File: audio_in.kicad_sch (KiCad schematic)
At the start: 17 parts, among them SW1 SW_SPDT

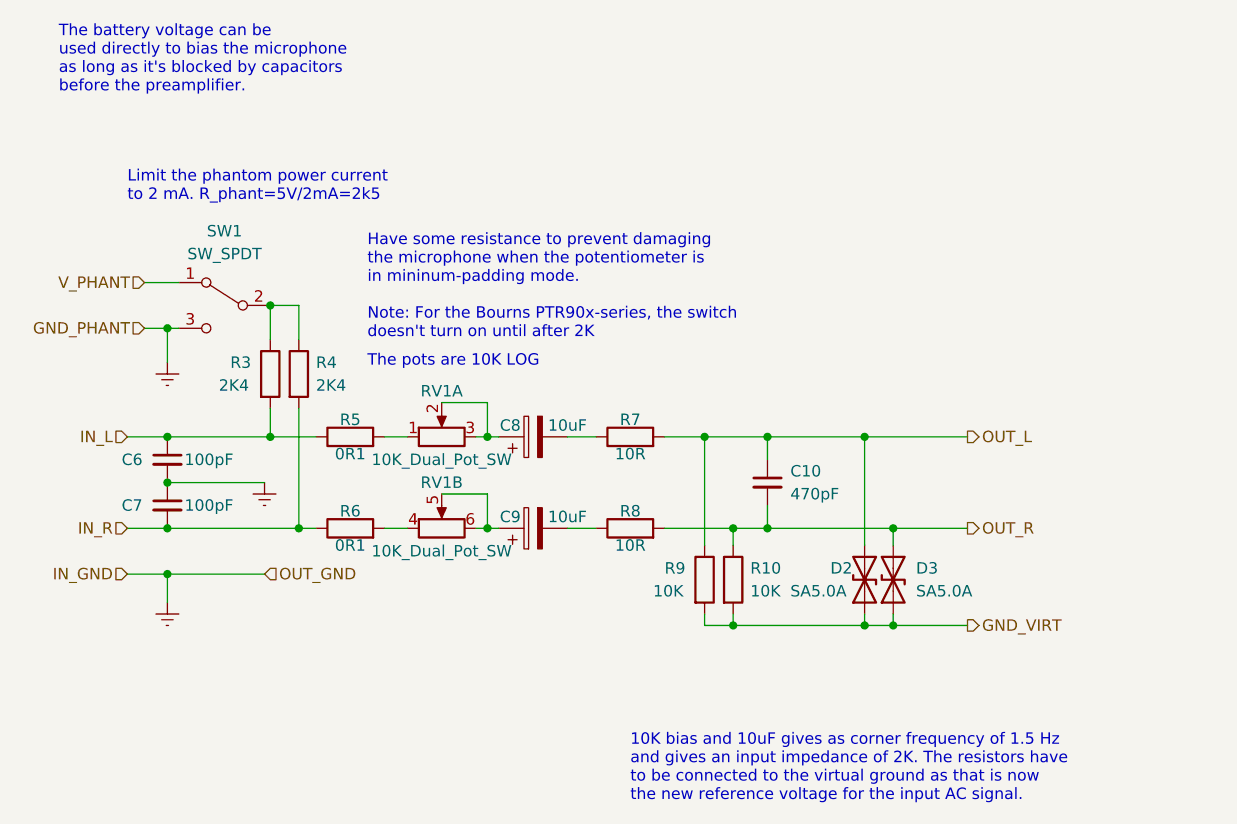
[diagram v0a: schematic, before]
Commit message: Almost finished 2-layer routing, not sure about power/ground layers though
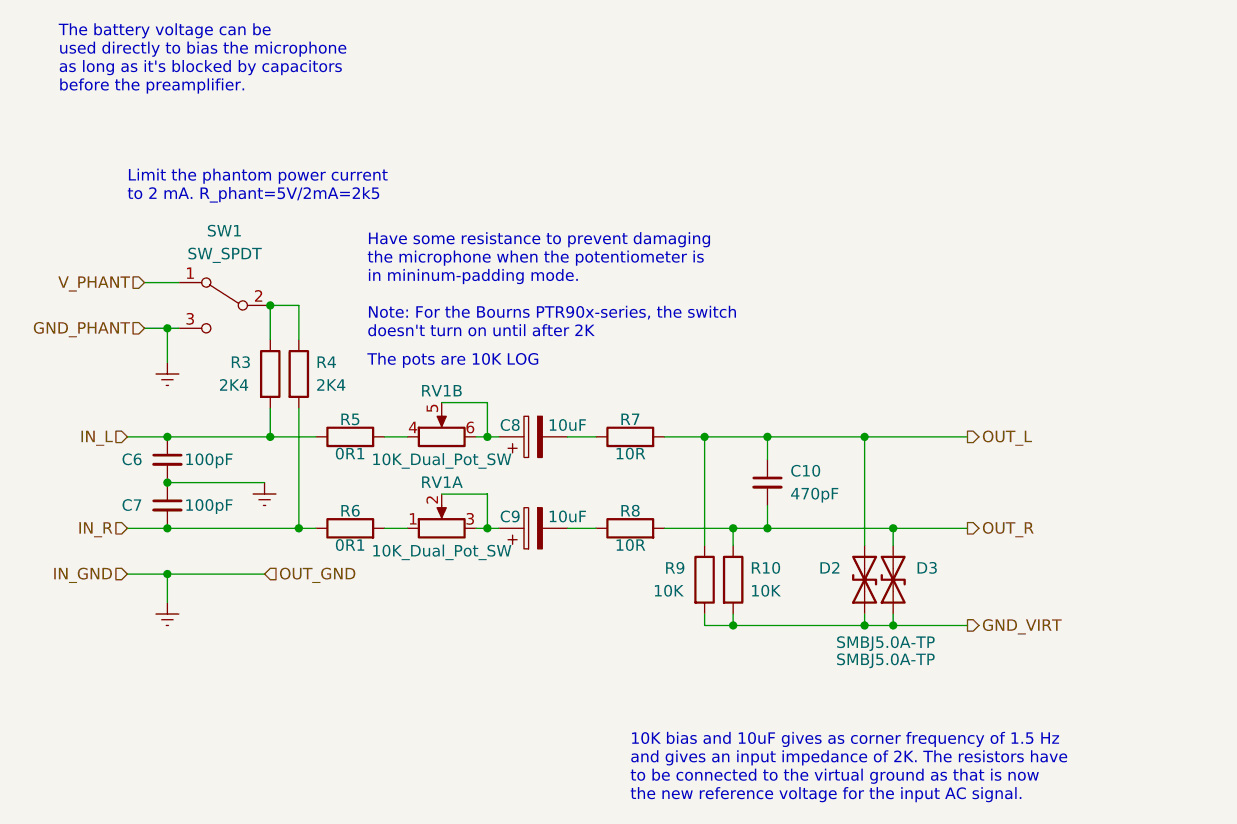
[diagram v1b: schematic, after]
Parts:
- removed D2, D3: SA5.0A, Diode_THT:D_5KP_P7.62mm_Vertical_KathodeUp, symbol preamp_lib:SA5.0A
- added D2, D3: SMBJ5.0A-TP, Diode_SMD:D_SMB_Handsoldering, symbol preamp_lib:SA9.0CA
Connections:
- net GND_VIRT: now also D2.1 (A1), D3.1 (A1)
- net OUT_L: now also D2.2 (A2)
- net OUT_R: now also D3.2 (A2)
- net at RV1.5, RV1.6: now also C8.1; no longer C9.1
- net at R6.2: now also RV1.1 (8); no longer RV1.4
- net at R5.2: now also RV1.4; no longer RV1.1 (8)
- net at RV1.2, RV1.3 (7): now also C9.1; no longer C8.1
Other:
- moved on the sheet: RV1A, RV1B
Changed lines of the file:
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@@
+    (pin "2")
+  )
+  (symbol (lib_id "preamp_lib:SA9.0CA") (at 132.08 81.28 90) (unit 1)
+    (in_bom yes) (on_board yes)
+    (property "Reference" "D3" (id 0) (at 134.62 80.0099 90)
+      (effects (font (size 1.27 1.27)) (justify right))
+    )
+    (property "Value" "SMBJ5.0A-TP" (id 1) (at 125.73 88.265 90)
+      (effects (font (size 1.27 1.27)) (justify right))
+    )
+    (property "Footprint" "Diode_SMD:D_SMB_Handsoldering" (id 2) (at 132.08 81.28 0)
+      (effects (font (size 1.27 1.27)) hide)
+    )
+    (property "Datasheet" "~" (id 3) (at 132.08 81.28 0)
+      (effects (font (size 1.27 1.27)) hide)
+    )
+    (pin "1")
     (pin "2")
   )
@@
     (pin "1")
   )
-  (symbol (lib_id "preamp_lib:SA5.0A") (at 128.905 81.28 90) (unit 1)
+  (symbol (lib_id "preamp_lib:SA9.0CA") (at 128.905 81.28 90) (unit 1)
     (in_bom yes) (on_board yes)
-    (property "Reference" "D2" (id 0) (at 125.095 80.01 90)
+    (property "Reference" "D2" (id 0) (at 123.825 80.01 90)
       (effects (font (size 1.27 1.27)) (justify right))
     )
-    (property "Value" "SA5.0A" (id 1) (at 120.65 82.55 90)
+    (property "Value" "SMBJ5.0A-TP" (id 1) (at 125.73 90.17 90)
       (effects (font (size 1.27 1.27)) (justify right))
     )
-    (property "Footprint" "Diode_THT:D_5KP_P7.62mm_Vertical_KathodeUp" (id 2) (at 128.905 81.28 0)
+    (property "Footprint" "Diode_SMD:D_SMB_Handsoldering" (id 2) (at 128.905 81.28 0)
       (effects (font (size 1.27 1.27)) hide)
     )
@@
     (pin "2")
   )
-  (symbol (lib_id "preamp_lib:SA5.0A") (at 132.08 81.28 90) (unit 1)
-    (in_bom yes) (on_board yes) (fields_autoplaced)
-    (property "Reference" "D3" (id 0) (at 134.62 80.0099 90)
-      (effects (font (size 1.27 1.27)) (justify right))
-    )
-    (property "Value" "SA5.0A" (id 1) (at 134.62 82.5499 90)
-      (effects (font (size 1.27 1.27)) (justify right))
-    )
-    (property "Footprint" "Diode_THT:D_5KP_P7.62mm_Vertical_KathodeUp" (id 2) (at 132.08 81.28 0)
-      (effects (font (size 1.27 1.27)) hide)
-    )
-    (property "Datasheet" "~" (id 3) (at 132.08 81.28 0)
-      (effects (font (size 1.27 1.27)) hide)
-    )
-    (pin "1")
-    (pin "2")
-  )
   (symbol (lib_id "Device:C_Small") (at 118.11 70.485 0) (unit 1)
     (in_bom yes) (on_board yes) (fields_autoplaced)
@@
     (pin "2")
   )
-  (symbol (lib_id "preamp_lib:10K_Dual_Pot_SW") (at 81.915 75.565 90) (unit 2)
+  (symbol (lib_id "preamp_lib:10K_Dual_Pot_SW") (at 81.915 65.405 90) (unit 2)
     (in_bom yes) (on_board yes)
-    (property "Reference" "RV1" (id 0) (at 81.915 70.485 90))
-    (property "Value" "10K_Dual_Pot_SW" (id 1) (at 81.915 78.105 90))
-    (property "Footprint" "preamp_footprints:Potentiometer_Bourns_PTR902_Double_Horizontal_Switch" (id 2) (at 81.915 75.565 0)
+    (property "Reference" "RV1" (id 0) (at 81.915 60.325 90))
+    (property "Value" "10K_Dual_Pot_SW" (id 1) (at 81.915 67.945 90))
+    (property "Footprint" "preamp_footprints:Potentiometer_Bourns_PTR902_Double_Horizontal_Switch" (id 2) (at 81.915 65.405 0)
       (effects (font (size 1.27 1.27)) hide)
     )
-    (property "Datasheet" "~" (id 3) (at 81.915 75.565 0)
+    (property "Datasheet" "~" (id 3) (at 81.915 65.405 0)
       (effects (font (size 1.27 1.27)) hide)
     )
@@
     (pin "8")
   )
-  (symbol (lib_id "preamp_lib:10K_Dual_Pot_SW") (at 81.915 65.405 90) (unit 1)
+  (symbol (lib_id "preamp_lib:10K_Dual_Pot_SW") (at 81.915 75.565 90) (unit 1)
     (in_bom yes) (on_board yes)
-    (property "Reference" "RV1" (id 0) (at 81.915 60.325 90))
-    (property "Value" "10K_Dual_Pot_SW" (id 1) (at 81.915 67.945 90))
-    (property "Footprint" "preamp_footprints:Potentiometer_Bourns_PTR902_Double_Horizontal_Switch" (id 2) (at 81.915 65.405 0)
+    (property "Reference" "RV1" (id 0) (at 81.915 70.485 90))
+    (property "Value" "10K_Dual_Pot_SW" (id 1) (at 81.915 78.105 90))
+    (property "Footprint" "preamp_footprints:Potentiometer_Bourns_PTR902_Double_Horizontal_Switch" (id 2) (at 81.915 75.565 0)
       (effects (font (size 1.27 1.27)) hide)
     )
-    (property "Datasheet" "~" (id 3) (at 81.915 65.405 0)
+    (property "Datasheet" "~" (id 3) (at 81.915 75.565 0)
       (effects (font (size 1.27 1.27)) hide)
     )
